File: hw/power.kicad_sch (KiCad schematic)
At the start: 55 parts, among them J9 Expansion, U1 RT8096B, U2 RT8096B, U25 TLV75801PDBV, U3 RT8096B, U5 TPS563249DDC

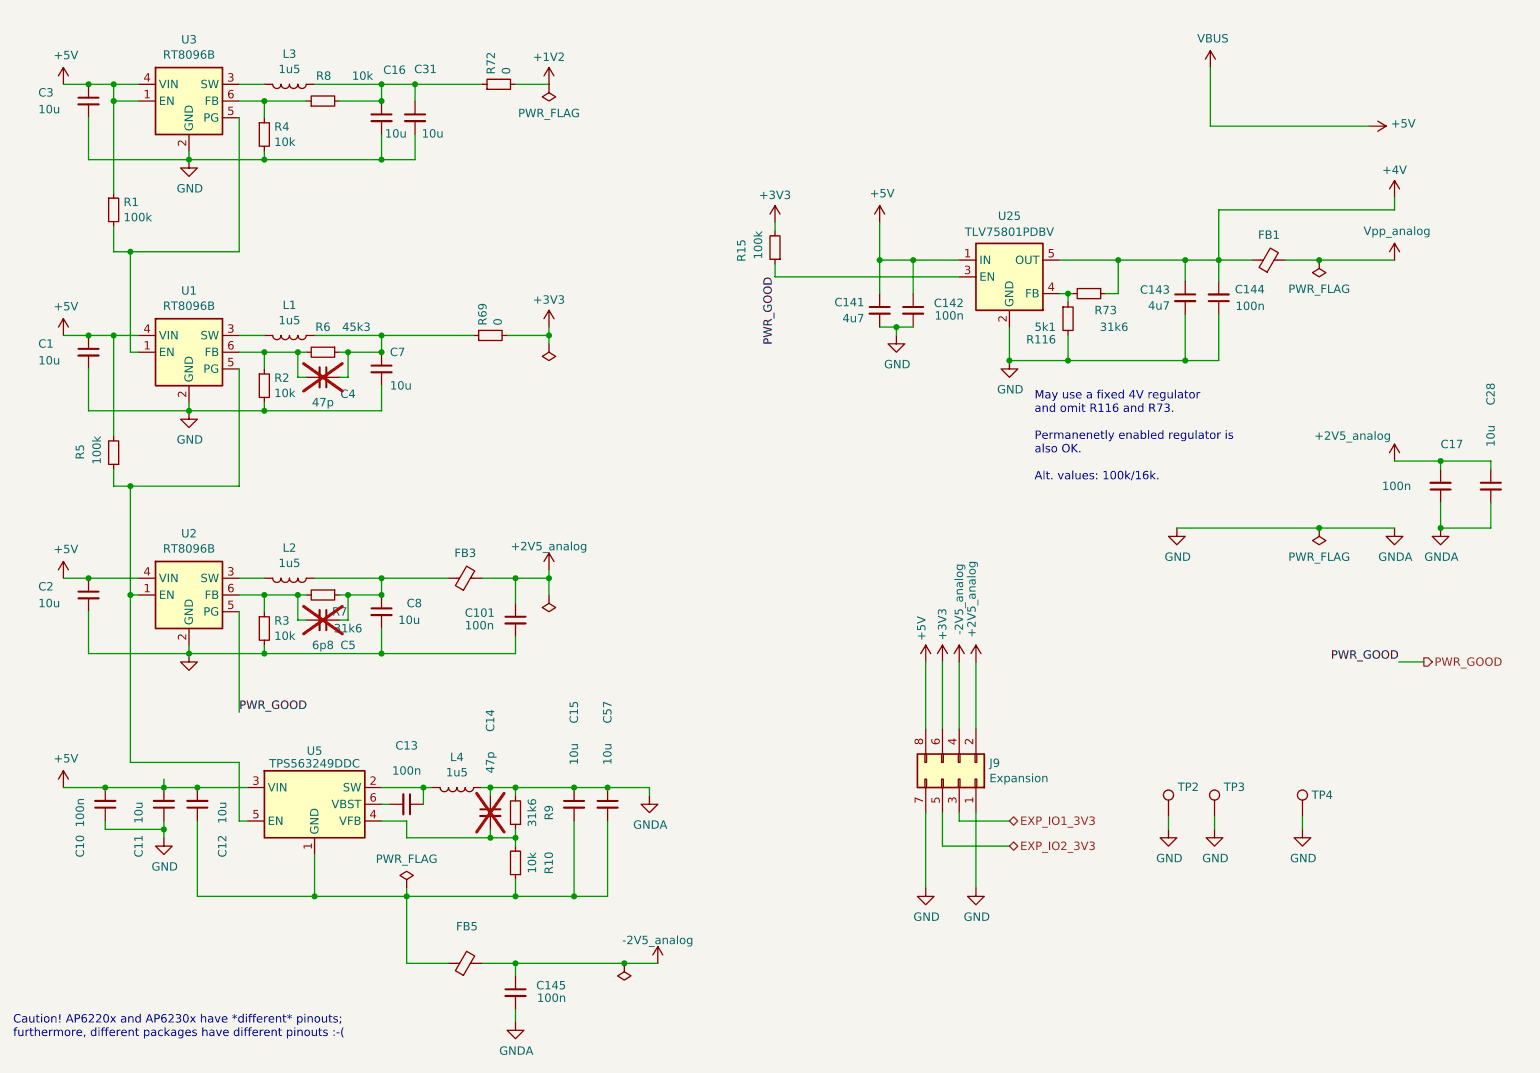
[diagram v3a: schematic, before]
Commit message: [hw] increased bypass caps on analog +/- supplies
Caps behind ferrite beads increased from 100n to 1u.
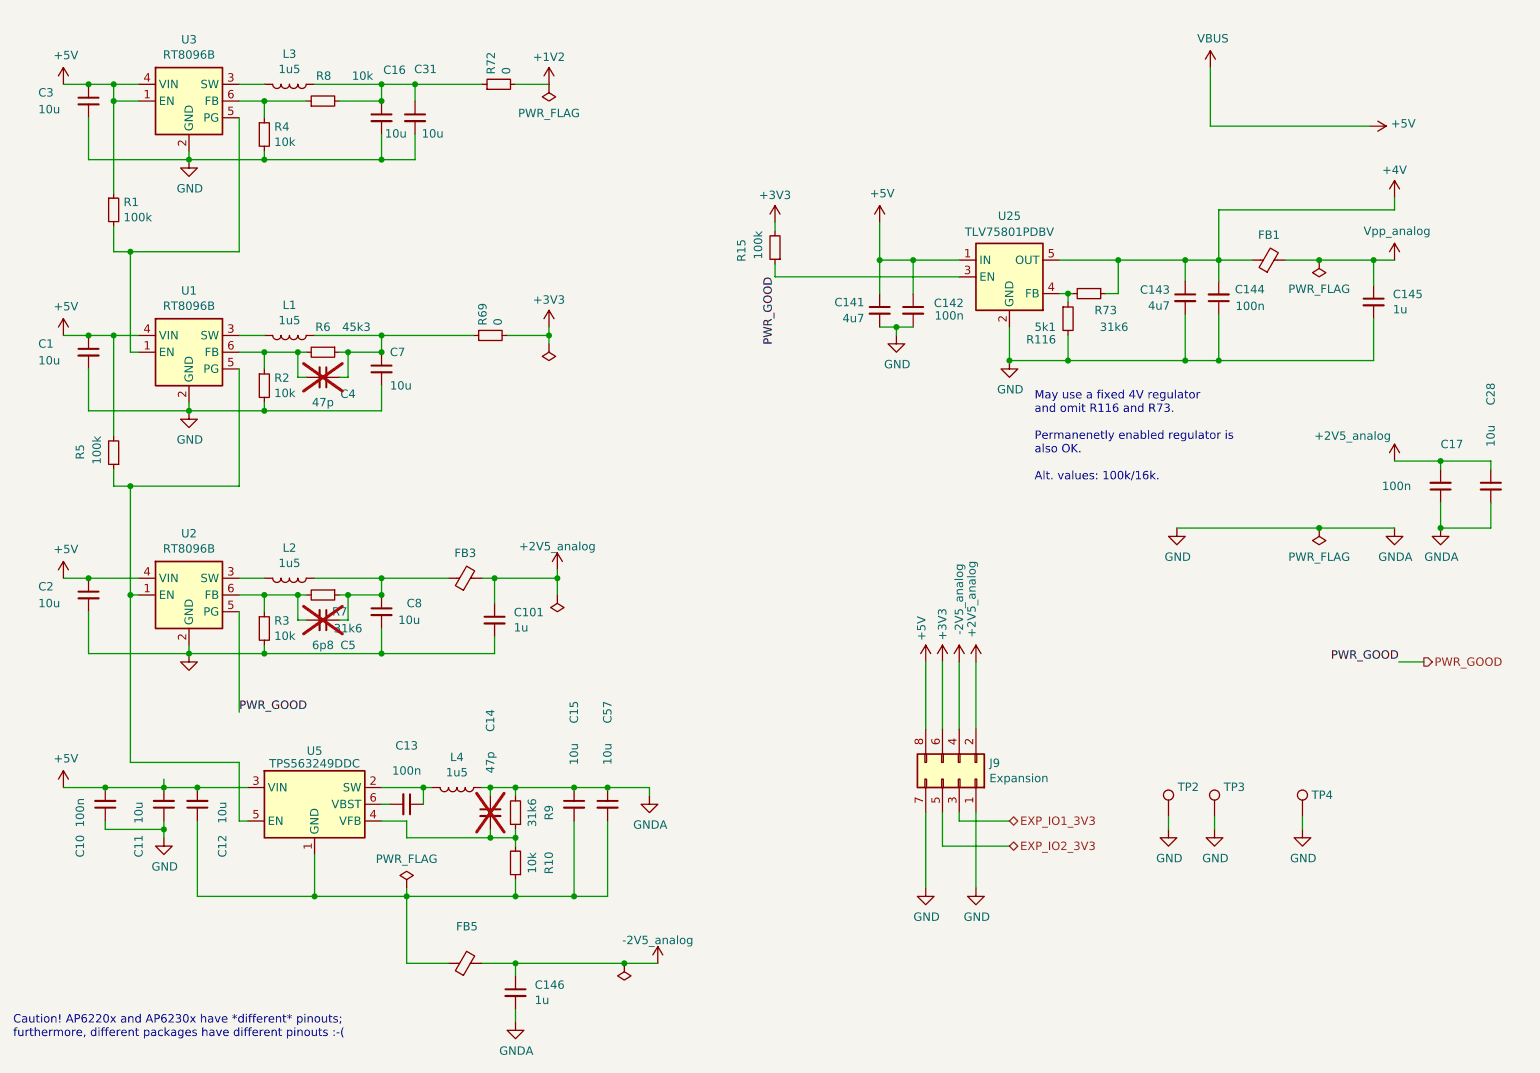
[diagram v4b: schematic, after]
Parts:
- added C146: 1u, Capacitor_SMD:C_0805_2012Metric, symbol Device:C_Small
- C101, C145: value 100n -> 1u; footprint Capacitor_SMD:C_0603_1608Metric -> Capacitor_SMD:C_0805_2012Metric; Manufacturer Samsung -> TDK; Part CL10B104KB8NFN -> CGA4J2X7R1C105K125AA
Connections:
- net -2V5_analog: now also C146.1; no longer C145.1
- net GND: now also C146.2
- net Vpp_analog: now also C145.1

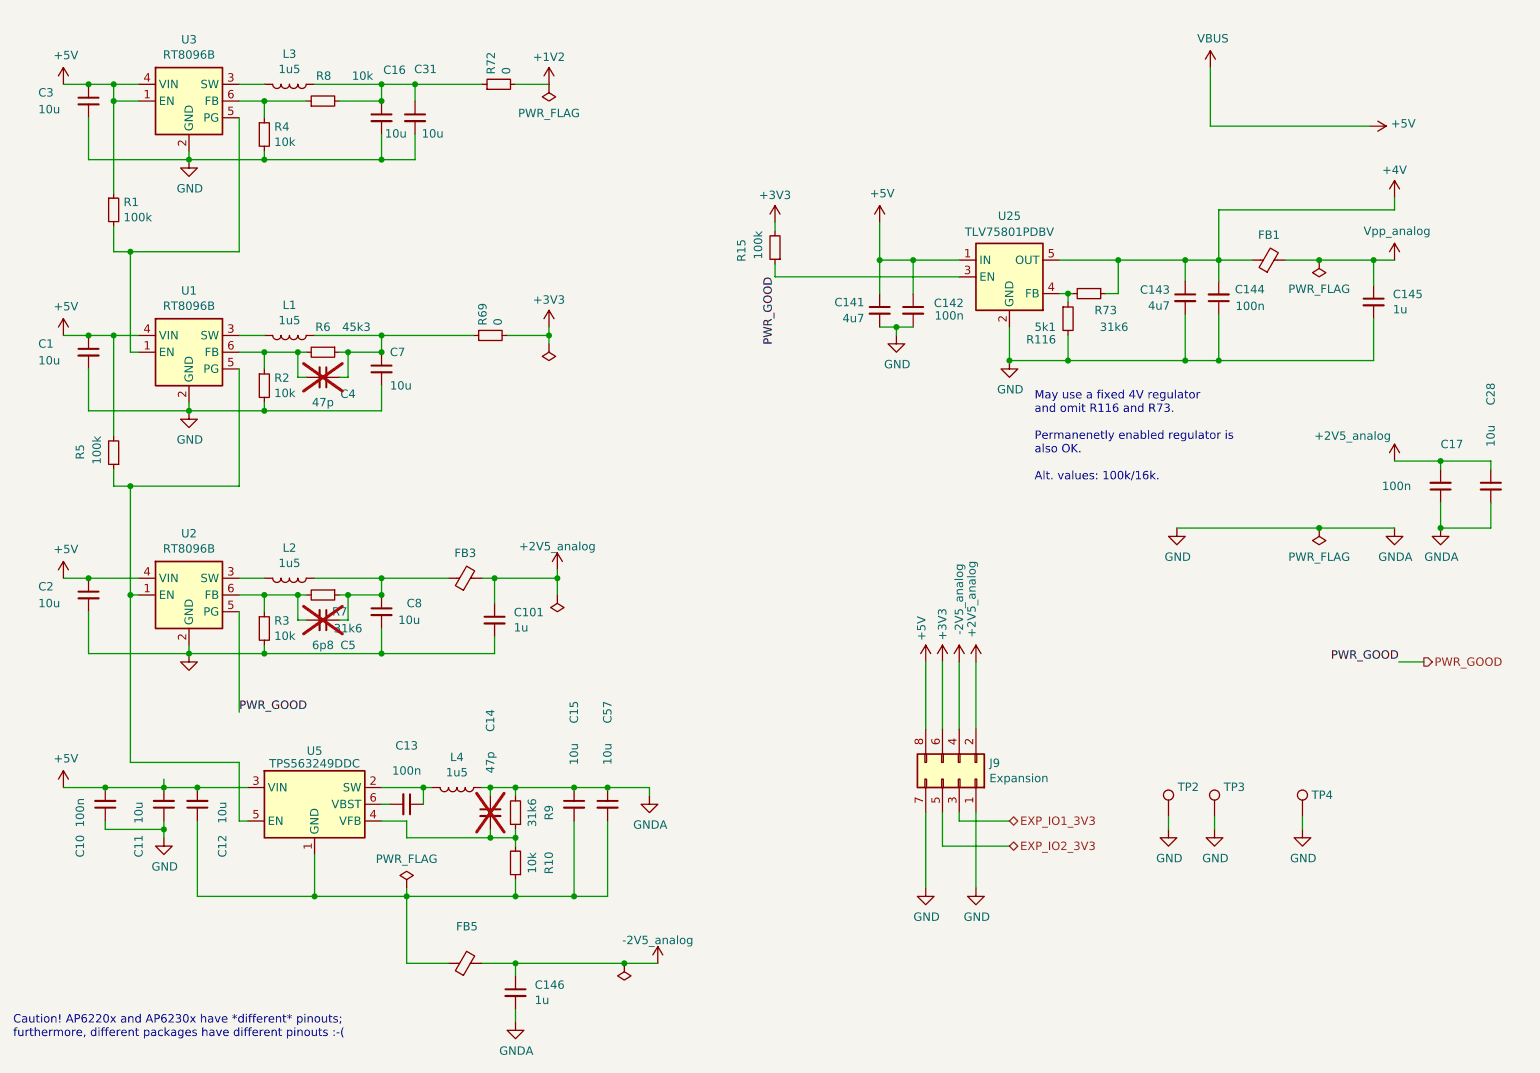
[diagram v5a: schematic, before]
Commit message: Modifications to power-supply: noise improvements
- DNL C12 (cap between 5V input and -2V5); created a bypass for noise
  coming into 5V. Improved spectrum up to ~200kHz, reducing spurs.
- Enabled C14 (feedback-zero for -2V5 regulator); reduce spurs (unstabilities?)
- DNL C145 (1u cap after ferrite bead isolating Vpp_analog.
- Replaced Vpp_analog isolation FB1 by a 10k resistor (R126)

The bead FB1 behaves as an 2uH inductor at low freq. The LC filter
formed by FB1 and decoupling caps is drastically underdamped by the
weak load (only analog switches) and enhances noise in the 10k-200k
band (depending on caps; particularly bad if C145 is loaded).
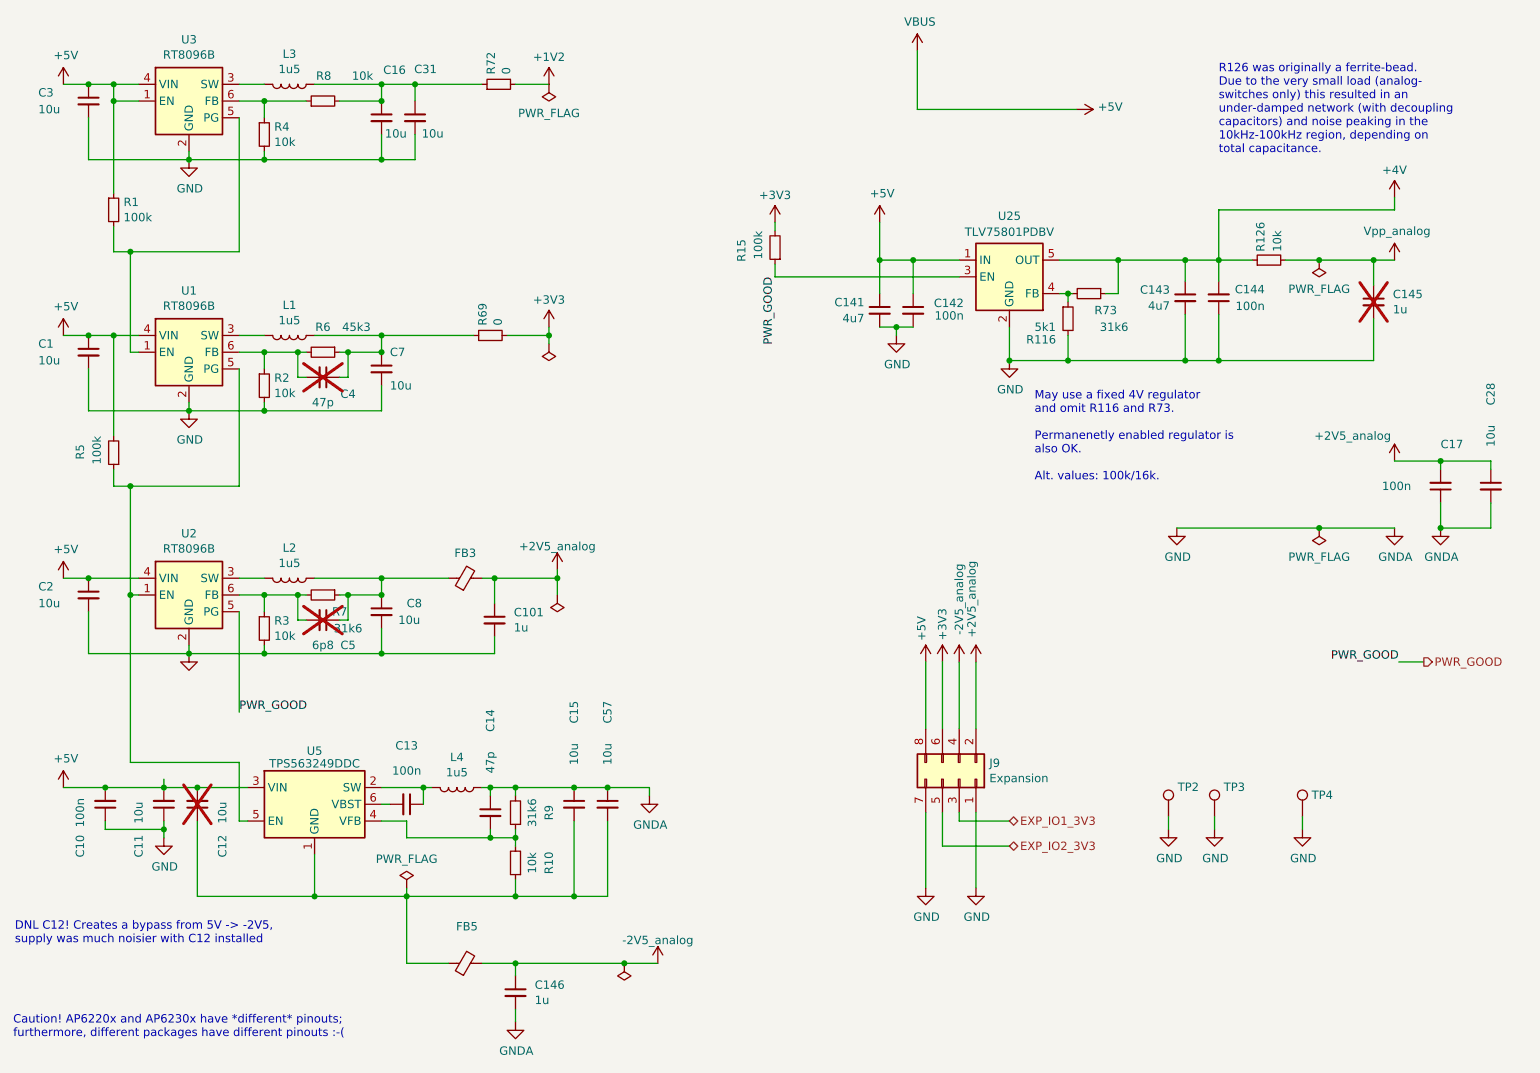
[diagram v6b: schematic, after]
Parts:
- removed FB1: 600Ohm@100MHz, Inductor_SMD:L_0603_1608Metric, symbol Device:FerriteBead_Small
- added R126: 10k, Resistor_SMD:R_0603_1608Metric, symbol Device:R_Small
- C12, C145: now not fitted; now left out of the parts list
- C14: now fitted; now in the parts list
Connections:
- net +4V: now also R126.1
- net Vpp_analog: now also R126.2
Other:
- note added: "DNL C12! Creates a bypass from 5V -> -2V5, supply was much noisier with C12 installed"
- note added: "R126 was originally a ferrite-bead. Due to the very small load (analog- switches only) this resulted in an under-damped network (with decoupling capacitors) and noise peaking in the 10kHz-100kHz region, depending on total capacitance."
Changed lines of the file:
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@@
 	(wire
 		(pts
-			(xy 224.79 29.21) (xy 224.79 38.1)
+			(xy 180.34 26.67) (xy 180.34 35.56)
 		)
 		(stroke
@@
 	(wire
 		(pts
-			(xy 224.79 38.1) (xy 248.92 38.1)
+			(xy 180.34 35.56) (xy 204.47 35.56)
 		)
 		(stroke
@@
 		)
 	)
+	(text "R126 was originally a ferrite-bead.\nDue to the very small load (analog-\nswitches only) this resulted in an\nunder-damped network (with decoupling\ncapacitors) and noise peaking in the\n10kHz-100kHz region, depending on\ntotal capacitance."
+		(exclude_from_sim no)
+		(at 226.06 35.56 0)
+		(effects
+			(font
+				(size 1.27 1.27)
+			)
+			(justify left)
+		)
+	)
+	(text "DNL C12! Creates a bypass from 5V -> -2V5,\nsupply was much noisier with C12 installed"
+		(exclude_from_sim no)
+		(at 43.434 160.528 0)
+		(effects
+			(font
+				(size 1.27 1.27)
+			)
+			(justify left)
+		)
+	)
 	(text "Caution! AP6220x and AP6230x have *different* pinouts;\nfurthermore, different packages have different pinouts :-("
 		(exclude_from_sim no)
@@
 	(symbol
 		(lib_id "power:VBUS")
-		(at 224.79 29.21 0)
+		(at 180.34 26.67 0)
 		(unit 1)
 		(exclude_from_sim no)
@@
 		(dnp no)
 		(property "Reference" "#PWR0162"
-			(at 224.79 33.02 0)
+			(at 180.34 30.48 0)
 			(effects
 				(font
@@
 		)
 		(property "Value" "VBUS"
-			(at 225.171 24.8158 0)
+			(at 180.721 22.2758 0)
 			(effects
 				(font
@@
 		)
 		(property "Footprint" ""
-			(at 224.79 29.21 0)
+			(at 180.34 26.67 0)
 			(effects
 				(font
@@
 		)
 		(property "Datasheet" ""
-			(at 224.79 29.21 0)
+			(at 180.34 26.67 0)
 			(effects
 				(font
@@
 		)
 		(property "Description" ""
-			(at 224.79 29.21 0)
+			(at 180.34 26.67 0)
 			(effects
 				(font
@@
 	(symbol
 		(lib_id "power:+5V")
-		(at 248.92 38.1 270)
+		(at 204.47 35.56 270)
 		(mirror x)
 		(unit 1)
@@
 		(dnp no)
 		(property "Reference" "#PWR0163"
-			(at 245.11 38.1 0)
+			(at 200.66 35.56 0)
 			(effects
 				(font
@@
 		)
 		(property "Value" "+5V"
-			(at 252.1712 37.719 90)
+			(at 207.7212 35.179 90)
 			(effects
 				(font
@@
 		)
 		(property "Footprint" ""
-			(at 248.92 38.1 0)
+			(at 204.47 35.56 0)
 			(effects
 				(font
@@
 		)
 		(property "Datasheet" ""
-			(at 248.92 38.1 0)
+			(at 204.47 35.56 0)
 			(effects
 				(font
@@
 		)
 		(property "Description" ""
-			(at 248.92 38.1 0)
+			(at 204.47 35.56 0)
 			(effects
 				(font
@@
 	(symbol
 		(lib_id "Device:FerriteBead_Small")
-		(at 233.68 58.42 90)
-		(unit 1)
-		(exclude_from_sim no)
-		(in_bom yes)
-		(on_board yes)
-		(dnp no)
-		(property "Reference" "FB1"
-			(at 233.68 54.61 90)
-			(effects
-				(font
-					(size 1.27 1.27)
-				)
-			)
-		)
-		(property "Value" "600Ohm@100MHz"
-			(at 233.68 64.77 90)
-			(effects
-				(font
-					(size 1.27 1.27)
-				)
-				(hide yes)
-			)
-		)
-		(property "Footprint" "Inductor_SMD:L_0603_1608Metric"
-			(at 233.68 60.198 90)
-			(effects
-				(font
-					(size 1.27 1.27)
-				)
-				(hide yes)
-			)
-		)
-		(property "Datasheet" "~"
-			(at 233.68 58.42 0)
-			(effects
-				(font
-					(size 1.27 1.27)
-				)
-				(hide yes)
-			)
-		)
-		(property "Description" ""
-			(at 233.68 58.42 0)
-			(effects
-				(font
-					(size 1.27 1.27)
-				)
-				(hide yes)
-			)
-		)
-		(property "Part" "MI0603J601R-10"
-			(at 233.68 58.42 90)
-			(effects
-				(font
-					(size 1.27 1.27)
-				)
-				(hide yes)
-			)
-		)
-		(property "Manufacturer" "Laird"
-			(at 233.68 58.42 90)
-			(effects
-				(font
-					(size 1.27 1.27)
-				)
-				(hide yes)
-			)
-		)
-		(pin "1"
-		)
-		(pin "2"
-		)
-		(instances
-			(project "usbadc"
-				(path "/7c8a1f8d-8834-4c9b-aaae-1f231e9b09a1/00000000-0000-0000-0000-00006086f2e3"
-					(reference "FB1")
-					(unit 1)
-				)
-			)
-		)
-	)
-	(symbol
-		(lib_id "Device:FerriteBead_Small")
 		(at 111.76 106.68 90)
 		(unit 1)
@@
 	)
 	(symbol
+		(lib_id "Device:R_Small")
+		(at 233.68 58.42 90)
+		(unit 1)
+		(exclude_from_sim no)
+		(in_bom yes)
+		(on_board yes)
+		(dnp no)
+		(property "Reference" "R126"
+			(at 232.41 57.15 0)
+			(effects
+				(font
+					(size 1.27 1.27)
+				)
+				(justify left)
+			)
+		)
+		(property "Value" "10k"
+			(at 234.95 57.15 0)
+			(effects
+				(font
+					(size 1.27 1.27)
+				)
+				(justify left)
+			)
+		)
+		(property "Footprint" "Resistor_SMD:R_0603_1608Metric"
+			(at 233.68 58.42 0)
+			(effects
+				(font
+					(size 1.27 1.27)
+				)
+				(hide yes)
+			)
+		)
+		(property "Datasheet" "~"
+			(at 233.68 58.42 0)
+			(effects
+				(font
+					(size 1.27 1.27)
+				)
+				(hide yes)
+			)
+		)
+		(property "Description" ""
+			(at 233.68 58.42 0)
+			(effects
+				(font
+					(size 1.27 1.27)
+				)
+				(hide yes)
+			)
+		)
+		(pin "1"
+		)
+		(pin "2"
+		)
+		(instances
+			(project "usbadc"
+				(path "/7c8a1f8d-8834-4c9b-aaae-1f231e9b09a1/00000000-0000-0000-0000-00006086f2e3"
+					(reference "R126")
+					(unit 1)
+				)
+			)
+		)
+	)
+	(symbol
 		(lib_id "Device:C_Small")
 		(at 66.04 140.97 180)
@@
 		(unit 1)
 		(exclude_from_sim no)
-		(in_bom no)
+		(in_bom yes)
 		(on_board yes)
-		(dnp yes)
+		(dnp no)
 		(property "Reference" "C14"
 			(at 115.57 128.27 90)
@@
 		(unit 1)
 		(exclude_from_sim no)
-		(in_bom yes)
+		(in_bom no)
 		(on_board yes)
-		(dnp no)
+		(dnp yes)
 		(property "Reference" "C145"
 			(at 252.476 63.6016 0)
@@
 		(unit 1)
 		(exclude_from_sim no)
-		(in_bom yes)
+		(in_bom no)
 		(on_board yes)
-		(dnp no)
+		(dnp yes)
 		(property "Reference" "C12"
 			(at 74.93 147.32 90)
